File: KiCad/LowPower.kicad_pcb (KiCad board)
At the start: 2 copper layers, 19 x 29 mm, 36 parts, among them J1 Connector, J2 USB-C, J3 DC, U1 ESP32-WROOM-32, U2 FT231XQ, U4 LMR16006+FB

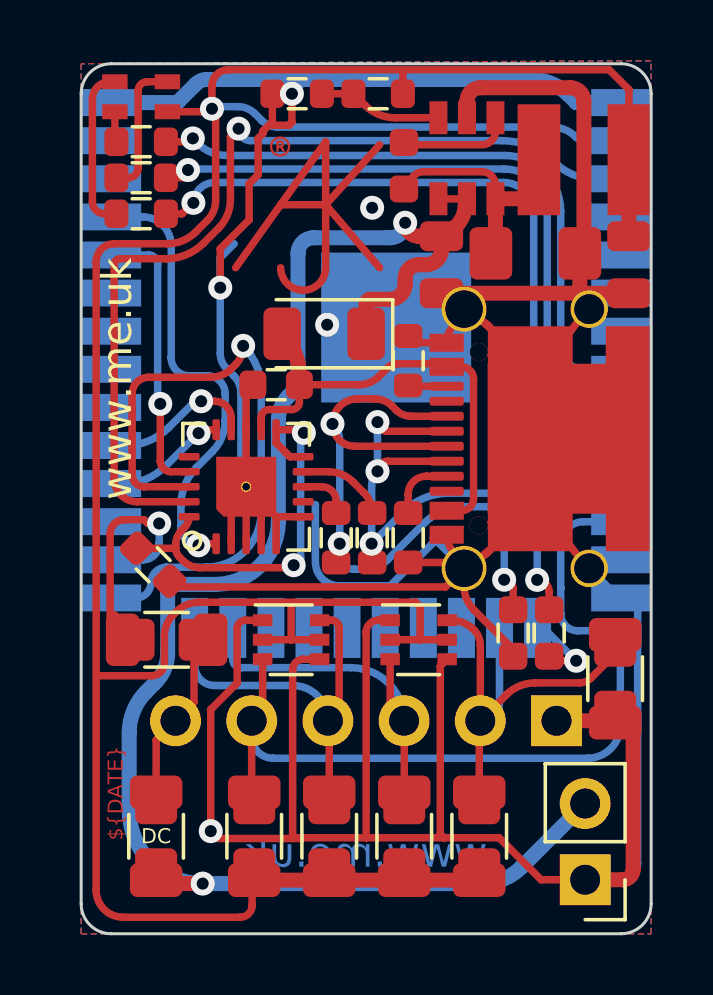
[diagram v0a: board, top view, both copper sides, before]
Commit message: Separate Generic and LowPower boards
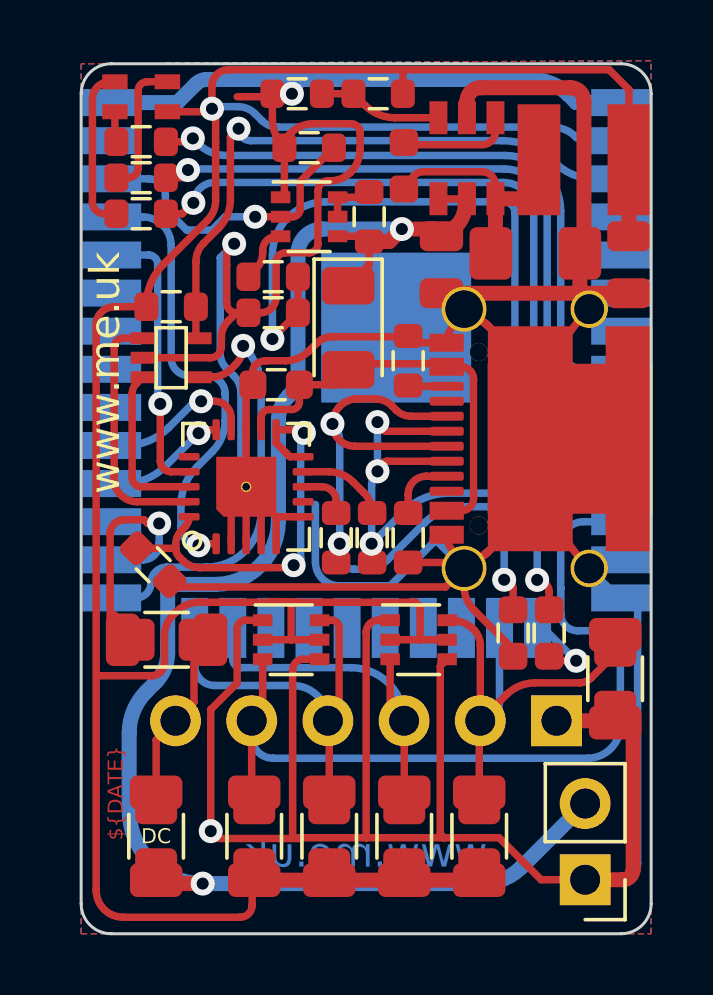
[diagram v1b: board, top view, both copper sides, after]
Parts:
- removed REF**: AJK, RevK:AJK
- added Q1: RN1701, RevK:USV-5, F.Cu at (120.2, 108.4)
- added R1: 10K, RevK:R_0603, F.Cu at (120.2, 106.7)
- added R15: 10K, RevK:R_0603, F.Cu at (124.8, 101.4)
- added R18: 10K, RevK:R_0603, F.Cu at (126.8, 103.7)
- added R19: 18K, RevK:R_0603, F.Cu at (123.6, 105.7)
- added R20: 1k, RevK:R_0603, F.Cu at (123.6, 106.9)
- added U3: NX6020CAKS, Package_TO_SOT_SMD:SOT-363_SC-70-6, F.Cu at (124.8, 103.7)
- moved D2 0.82 mm to (126.1, 107.4), turned to -90 degrees
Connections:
- U1 pad 11: unconnected-(U1-Pad11) -> ADC
- U1 pad 25: GPIO0 -> Net-(Q1-Pad4)
- U1 pad 3: EN -> Net-(Q1-Pad5)
- U1 pad 36: unconnected-(U1-Pad36) -> ADCON
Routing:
- net ADC: track 0.00 -> 26.0 mm, vias 0 -> 1
- net EN: track 30.8 -> 8.40 mm, vias 1 -> 0
- net GND: track 146.3 -> 167.9 mm, vias 6 -> 4
- net Net-(Q1-Pad5): track 0.00 -> 20.8 mm, vias 0 -> 1
- net GPIO0: track 21.6 -> 5.53 mm, vias 1 -> 0
- net Net-(Q1-Pad4): track 0.00 -> 14.2 mm, vias 0 -> 1
- net ADCON: track 0.00 -> 10.2 mm, vias 0 -> 1
- net Net-(R19-Pad1): track 0.00 -> 1.89 mm
- net Net-(R18-Pad1): track 0.00 -> 1.77 mm
- net VBUS: track 15.8 -> 14.0 mm
- net DC: track 52.3 -> 51.2 mm

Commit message: New bigger generic and tidy library
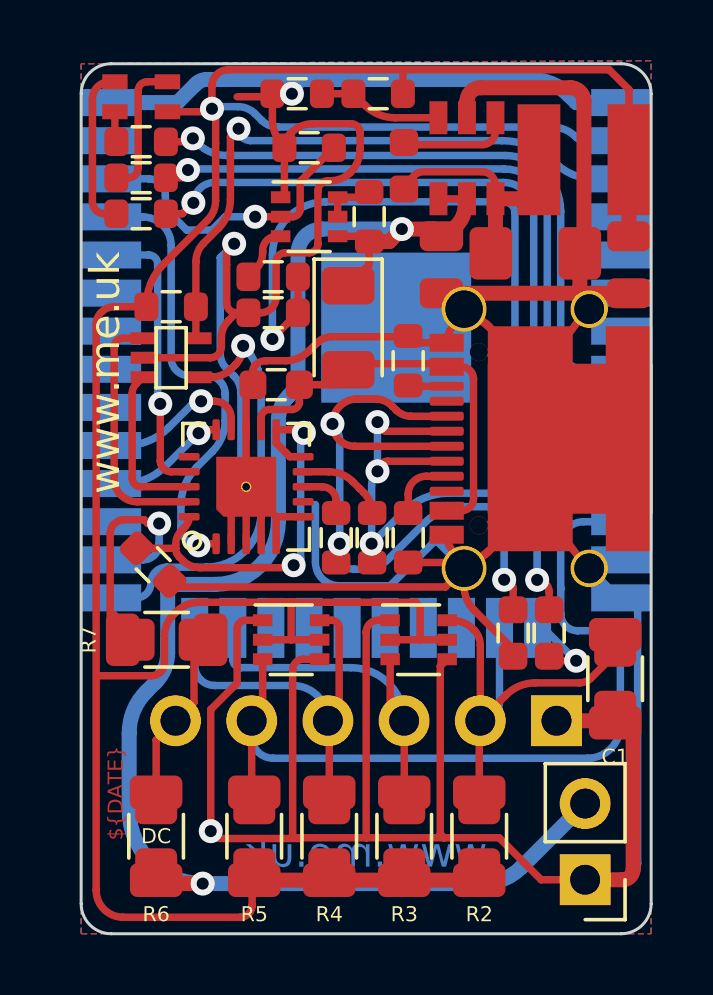
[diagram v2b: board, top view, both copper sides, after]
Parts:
- C1, R2, R3, R4, R5, R6, R7: footprint RevK:Pad_1206_0805_NF -> RevK:Pad_1206_0805_Open

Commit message: Lots of tidy - mainly silkscreen stuff
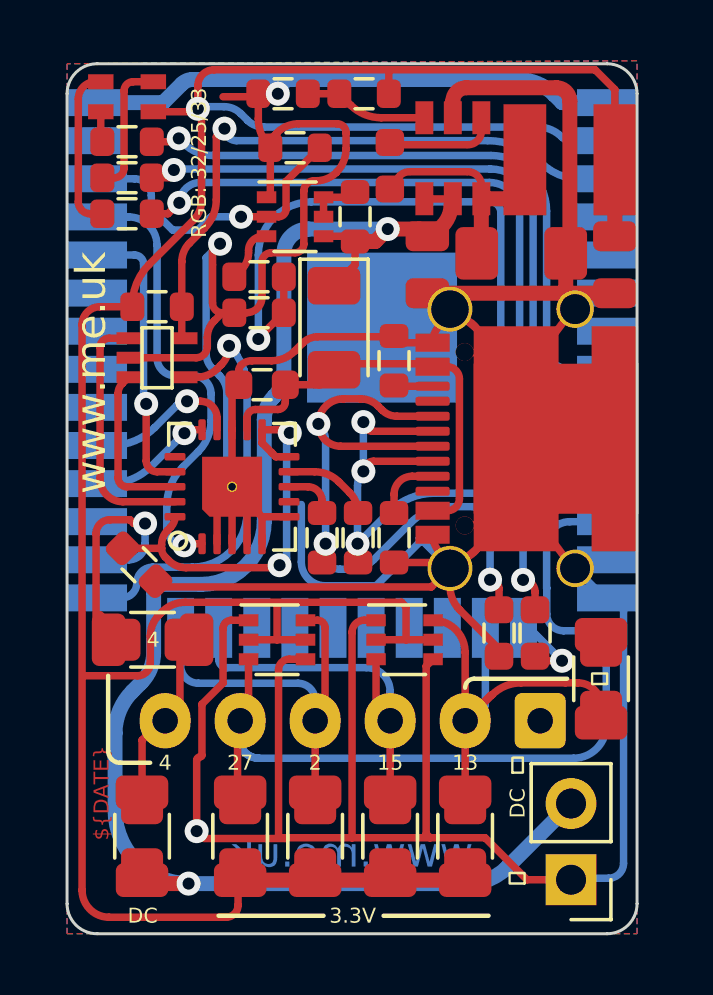
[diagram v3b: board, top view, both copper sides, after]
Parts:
- J1: footprint RevK:Molex_MiniSPOX_H6RA_0.1 -> RevK:Molex_MiniSPOX_H6RA
- R10: value 324R -> 330R
- R8: value 732R -> 680R
- moved C1 0.47 mm to (134.5, 119.1), turned to -90 degrees
- moved C2 0.47 mm to (119.1, 115.3)
- moved C3 0.47 mm to (132.3, 117.6)
- moved C4 0.47 mm to (131.1, 117.6)
- moved C5 0.47 mm to (123.2, 109.3)
- moved C6 0.47 mm to (127.5, 102.0)
- moved C7 0.47 mm to (128.7, 105.3)
- moved C8 0.47 mm to (135.0, 105.3)
- moved D1 0.47 mm to (118.7, 99.7)
- moved D2 0.47 mm to (125.6, 107.4)
- moved D4 0.47 mm to (123.7, 117.8)
- moved D5 0.47 mm to (131.9, 104.9)
- moved J1 0.47 mm to (126.2, 120.5)
- moved J2 0.47 mm to (135.8, 111.1)
- moved J3 0.47 mm to (133.5, 125.8)
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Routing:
- net GND: track 167.9 -> 157.9 mm
- net IO4: track 28.8 -> 30.4 mm
- net IO1: track 15.9 -> 17.4 mm
- net +3V3: track 95.9 -> 95.0 mm
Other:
- board text added: "3.3V"
- board text added: "5: CHARGER 17: USB 22: ADCON 26: ADC"
- board text added: "RGB: 32/25/33"
- board text added: "⏚"
- board text removed: "5: CHARGER 17: USB 22: ADCON 26: ADC 33: R 32: G 25: B"

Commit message: Footprint update
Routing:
- net GND: track 157.9 -> 149.3 mm, vias 4 -> 5
